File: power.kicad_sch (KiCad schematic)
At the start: 27 parts, among them Q1 CSD16321Q5, Q2 CSD16321Q5, Q9 BSS138, U1 TPS40304DRC

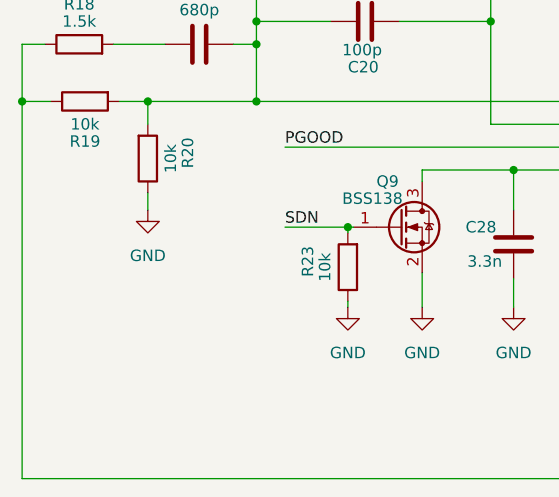
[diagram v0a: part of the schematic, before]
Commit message: revised heat-sinking. Supports heatsinks with 40x40 size with holes 35x35, 32x32 and 33x33
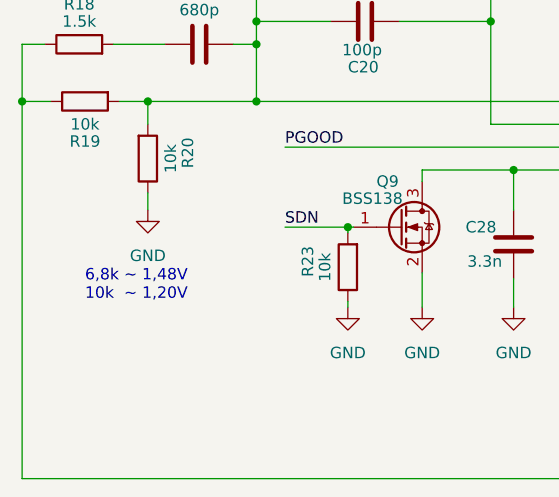
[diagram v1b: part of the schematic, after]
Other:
- note added: "6,8k ~ 1,48V 10k ~ 1,20V"
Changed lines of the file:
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@@
     (stroke (width 0) (type default))
+  )
+  (text "6,8k ~ 1,48V\n10k  ~ 1,20V" (at 57.785 133.35 0)
+    (effects (font (size 1.27 1.27)) (justify left bottom))
   )
   (label "PGOOD" (at 243.205 27.94 0) (fields_autoplaced)

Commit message: added gerbers and bom
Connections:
- net VIn: now also C27.1, U1.1 (VDD)
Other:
- moved on the sheet: C35, C36, C42

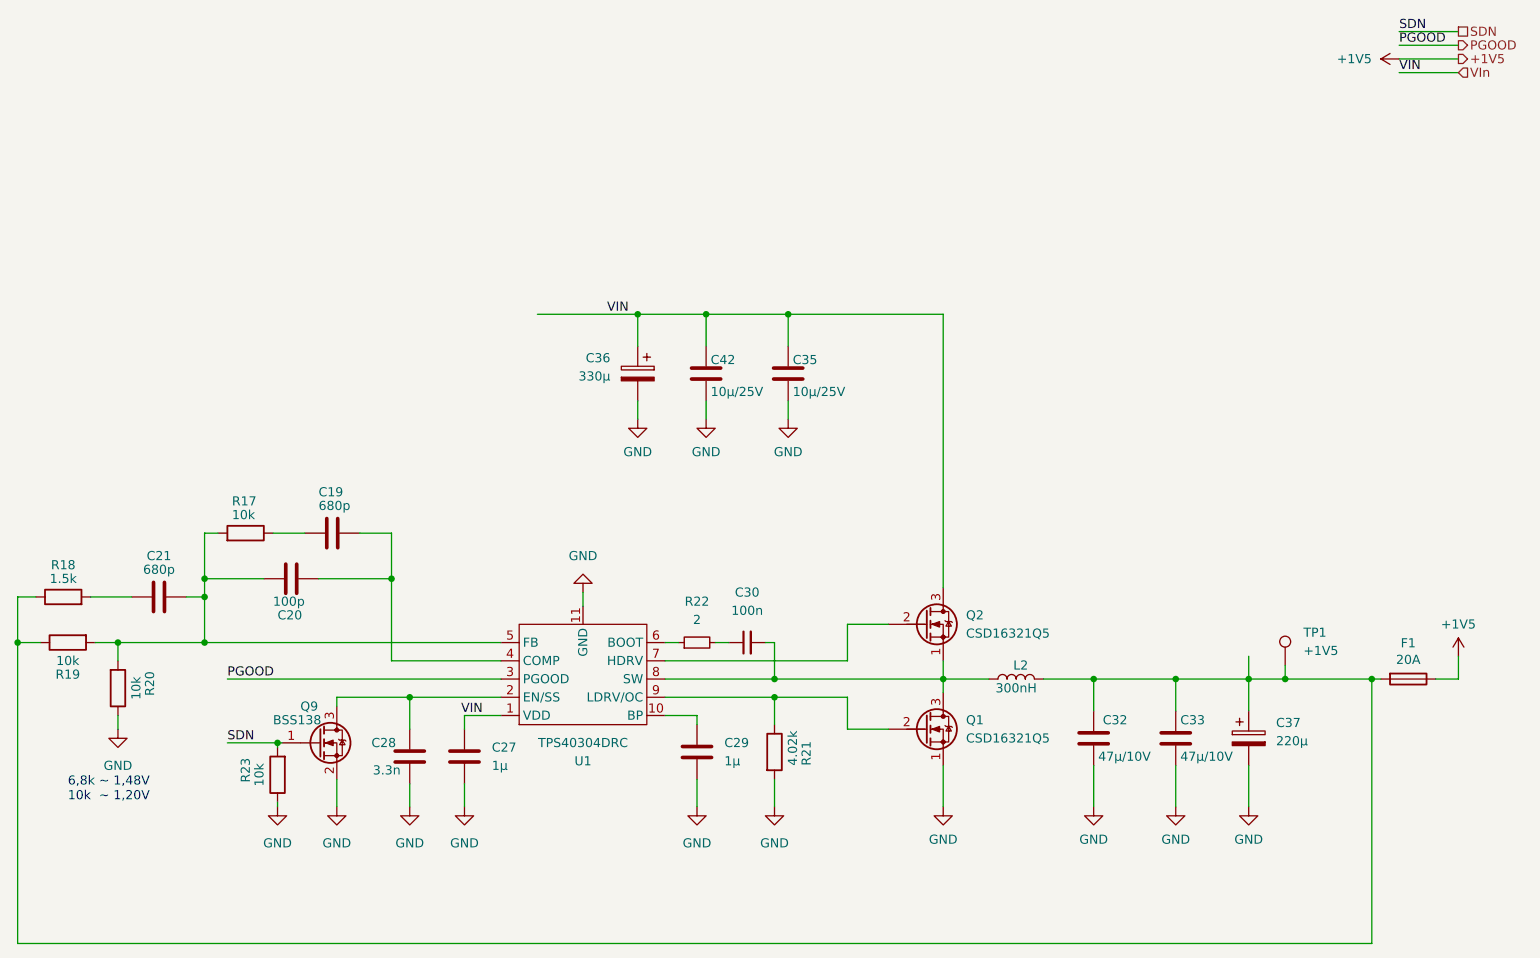
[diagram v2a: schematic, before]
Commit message: fixed zone-edgecut clearance, added 2nd gnd layer and stitched them together for copper balance
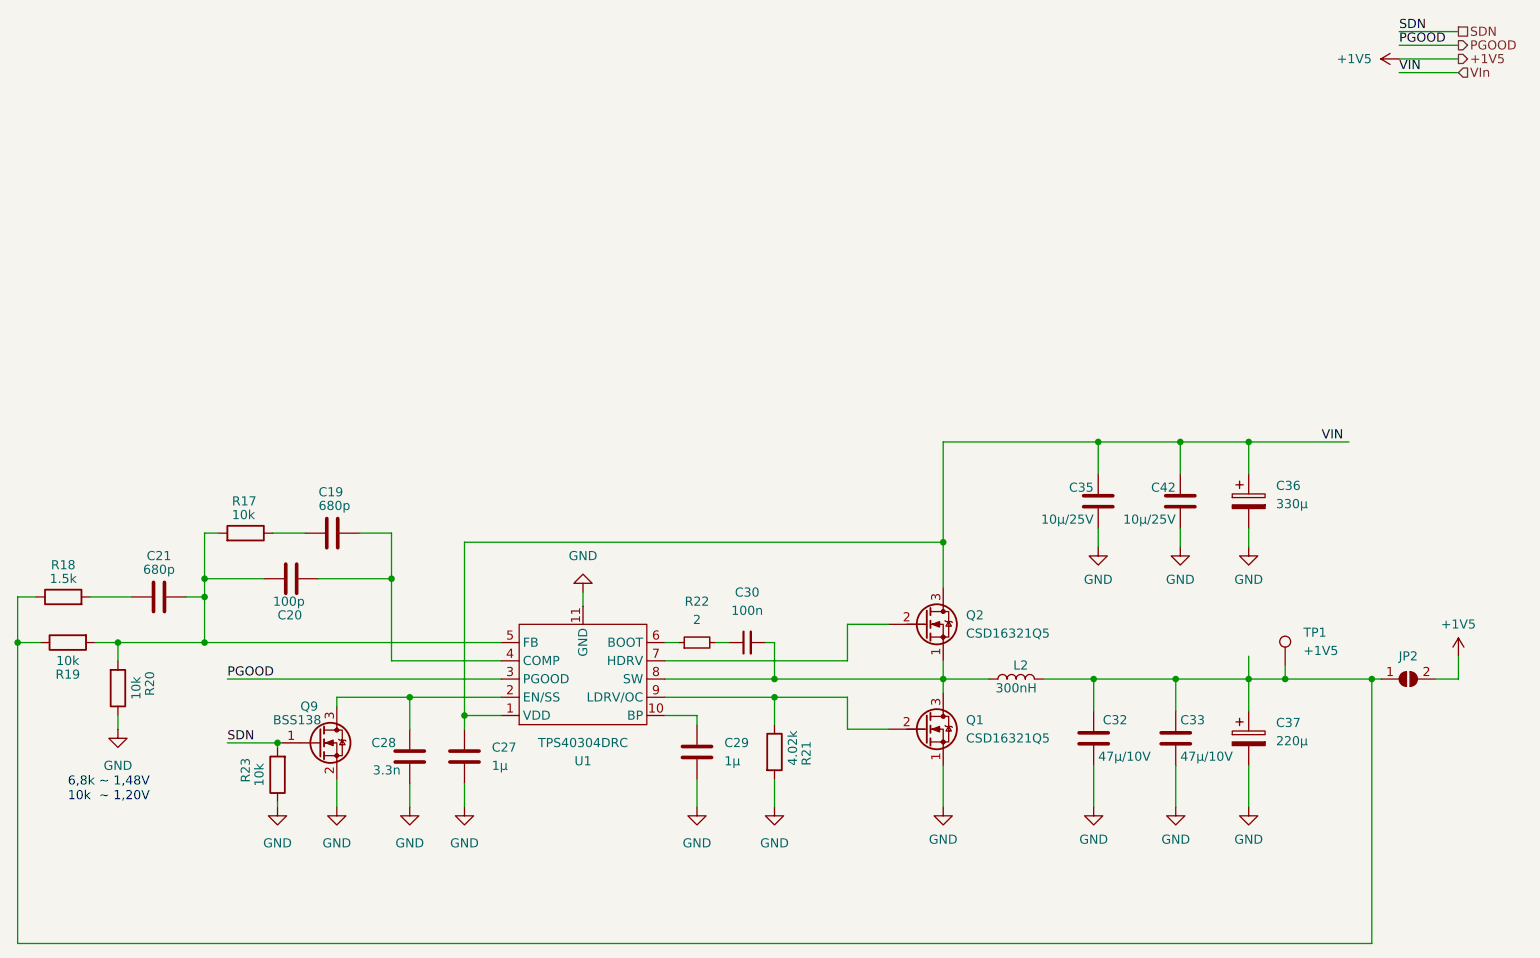
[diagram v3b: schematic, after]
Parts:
- removed F1: 20A, myfootprints:fuseholder_littlefuse_blok, symbol Device:Fuse
- added JP2: SolderJumper_2_Open, myfootprints:SolderJumper1.0x4.5, symbol Jumper:SolderJumper_2_Open
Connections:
- net +1V5: now also JP2.2 (B)
- net at C32.1, C33.1, C37.1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: now also JP2.1 (A)
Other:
- moved on the sheet: C35, C36, C42

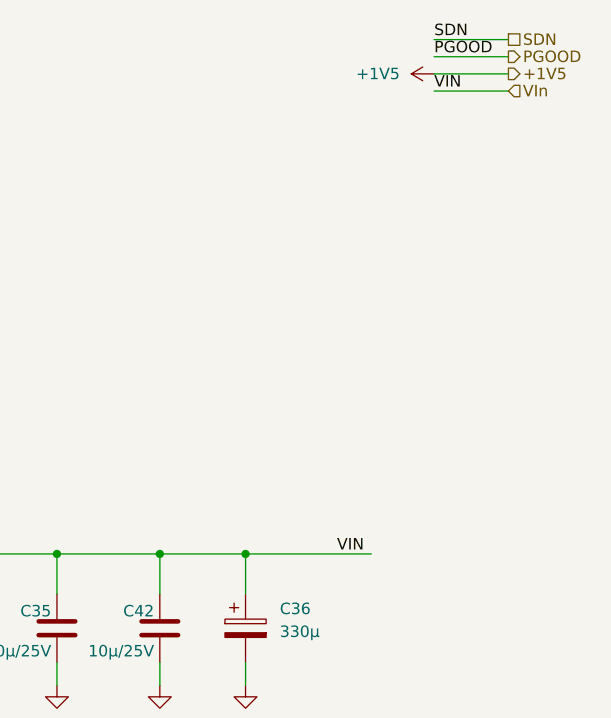
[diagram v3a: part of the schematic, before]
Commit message: removed useless snubber
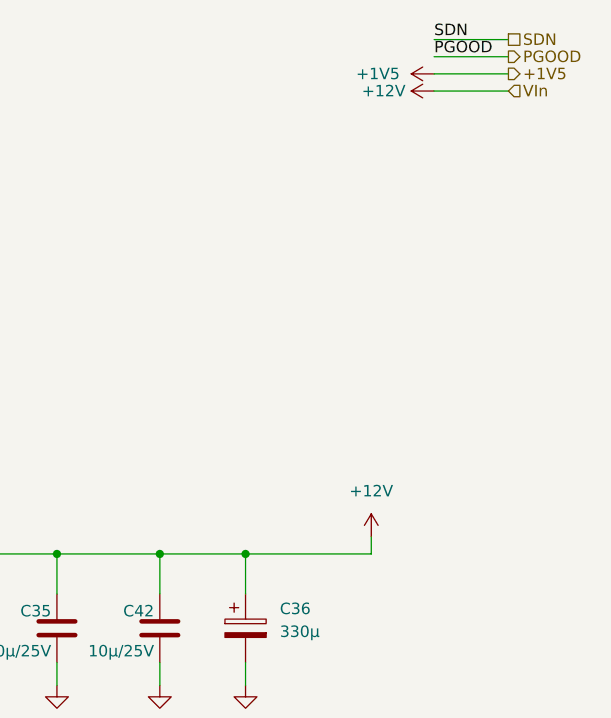
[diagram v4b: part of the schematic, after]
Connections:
- net VIn renamed +12V
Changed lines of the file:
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@@
+    (stroke (width 0) (type default))
+  )
+  (wire (pts (xy 236.22 81.28) (xy 236.22 83.185))
     (stroke (width 0) (type default))
   )
@@
     (effects (font (size 1.27 1.27)) (justify left bottom))
   )
-  (label "VIN" (at 232.41 83.185 0) (fields_autoplaced)
-    (effects (font (size 1.27 1.27)) (justify left bottom))
-  )
-  (label "VIN" (at 243.205 31.75 0) (fields_autoplaced)
-    (effects (font (size 1.27 1.27)) (justify left bottom))
-  )
   (label "PGOOD" (at 80.01 116.205 0) (fields_autoplaced)
     (effects (font (size 1.27 1.27)) (justify left bottom))
@@
         (path "/e63e39d7-6ac0-4ffd-8aa3-1841a4541b55/8ec0a9c6-2b78-44ef-a83d-9047d2828409"
           (reference "#PWR077") (unit 1)
+        )
+      )
+    )
+  )
+  (symbol (lib_id "power:+12V") (at 236.22 81.28 0) (unit 1)
+    (in_bom yes) (on_board yes) (dnp no) (fields_autoplaced)
+    (property "Reference" "#PWR09" (at 236.22 85.09 0)
+      (effects (font (size 1.27 1.27)) hide)
+    )
+    (property "Value" "+12V" (at 236.22 76.2 0)
+      (effects (font (size 1.27 1.27)))
+    )
+    (property "Footprint" "" (at 236.22 81.28 0)
+      (effects (font (size 1.27 1.27)) hide)
+    )
+    (property "Datasheet" "" (at 236.22 81.28 0)
+      (effects (font (size 1.27 1.27)) hide)
+    )
+    (pin "1")
+    (instances
+      (project "bitaxeUltra"
+        (path "/e63e39d7-6ac0-4ffd-8aa3-1841a4541b55/8ec0a9c6-2b78-44ef-a83d-9047d2828409"
+          (reference "#PWR09") (unit 1)
         )
       )
@@
         )
       )
+    )
+  )
+  (symbol (lib_id "power:+12V") (at 243.205 31.75 90) (unit 1)
+    (in_bom yes) (on_board yes) (dnp no) (fields_autoplaced)
+    (property "Reference" "#PWR011" (at 247.015 31.75 0)
+      (effects (font (size 1.27 1.27)) hide)
+    )
+    (property "Value" "+12V" (at 240.03 31.75 90)
+      (effects (font (size 1.27 1.27)) (justify left))
+    )
+    (property "Footprint" "" (at 243.205 31.75 0)
+      (effects (font (size 1.27 1.27)) hide)
+    )
+    (property "Datasheet" "" (at 243.205 31.75 0)
+      (effects (font (size 1.27 1.27)) hide)
+    )
+    (pin "1")
+    (instances
+      (project "bitaxeUltra"
+        (path "/e63e39d7-6ac0-4ffd-8aa3-1841a4541b55/8ec0a9c6-2b78-44ef-a83d-9047d2828409"
+          (reference "#PWR011") (unit 1)
+        )
+      )

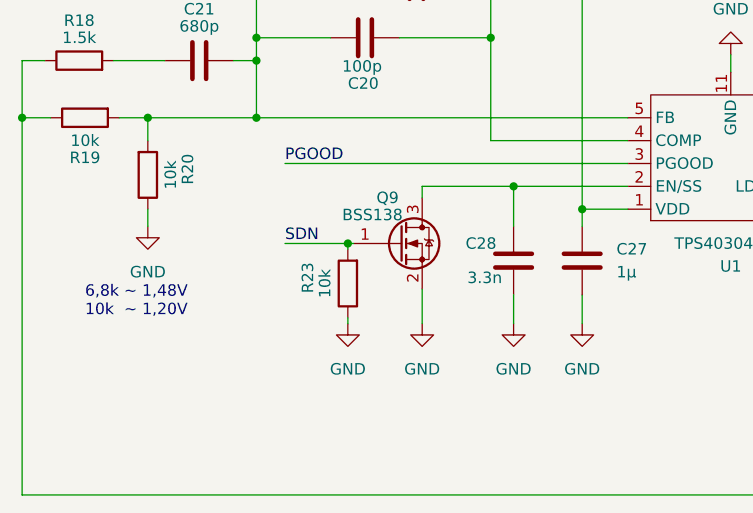
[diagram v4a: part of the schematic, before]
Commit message: fixed some order numbers, added initial python code for testing
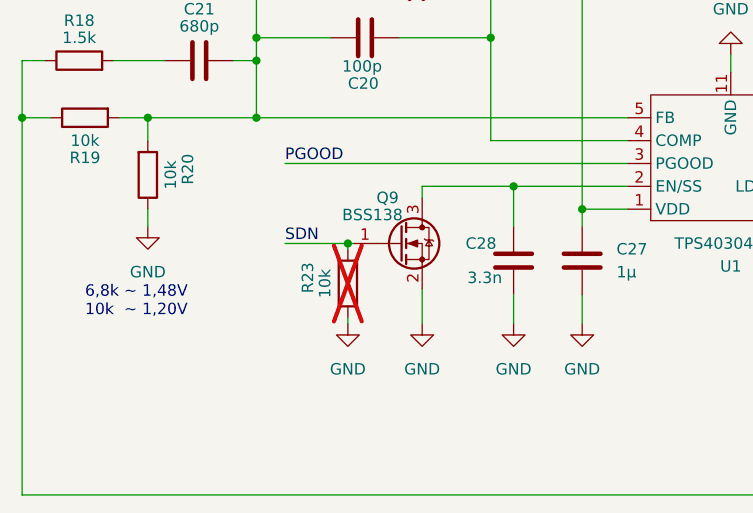
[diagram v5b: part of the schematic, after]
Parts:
- C36: Manufacturer EEE-FP1E331AP -> A768KS337M1ELAE019; OrderNr PCE4439CT-ND -> 399-A768KS337M1ELAE019CT-ND
- C37: Manufacturer EEE-FT0J221AR -> PCK0J221MCO1GS; OrderNr P15078CT-ND -> 493-3995-1-ND
- R23: now not fitted
